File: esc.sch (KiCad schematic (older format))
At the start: 37 parts, among them IC1 C8051F330/1, P1 CONN_01X01, P2 CONN_01X01, P3 CONN_01X01

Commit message: Initial commit
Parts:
- R18, R19, R20: renamed from R?; value 470 -> 330
- gave numbers to parts that had none: 30
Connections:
- net at P5.1 (P1), Q5.3 (D), R9.1: now also Q4.2 (D)
- no-connect marks 0 -> 4

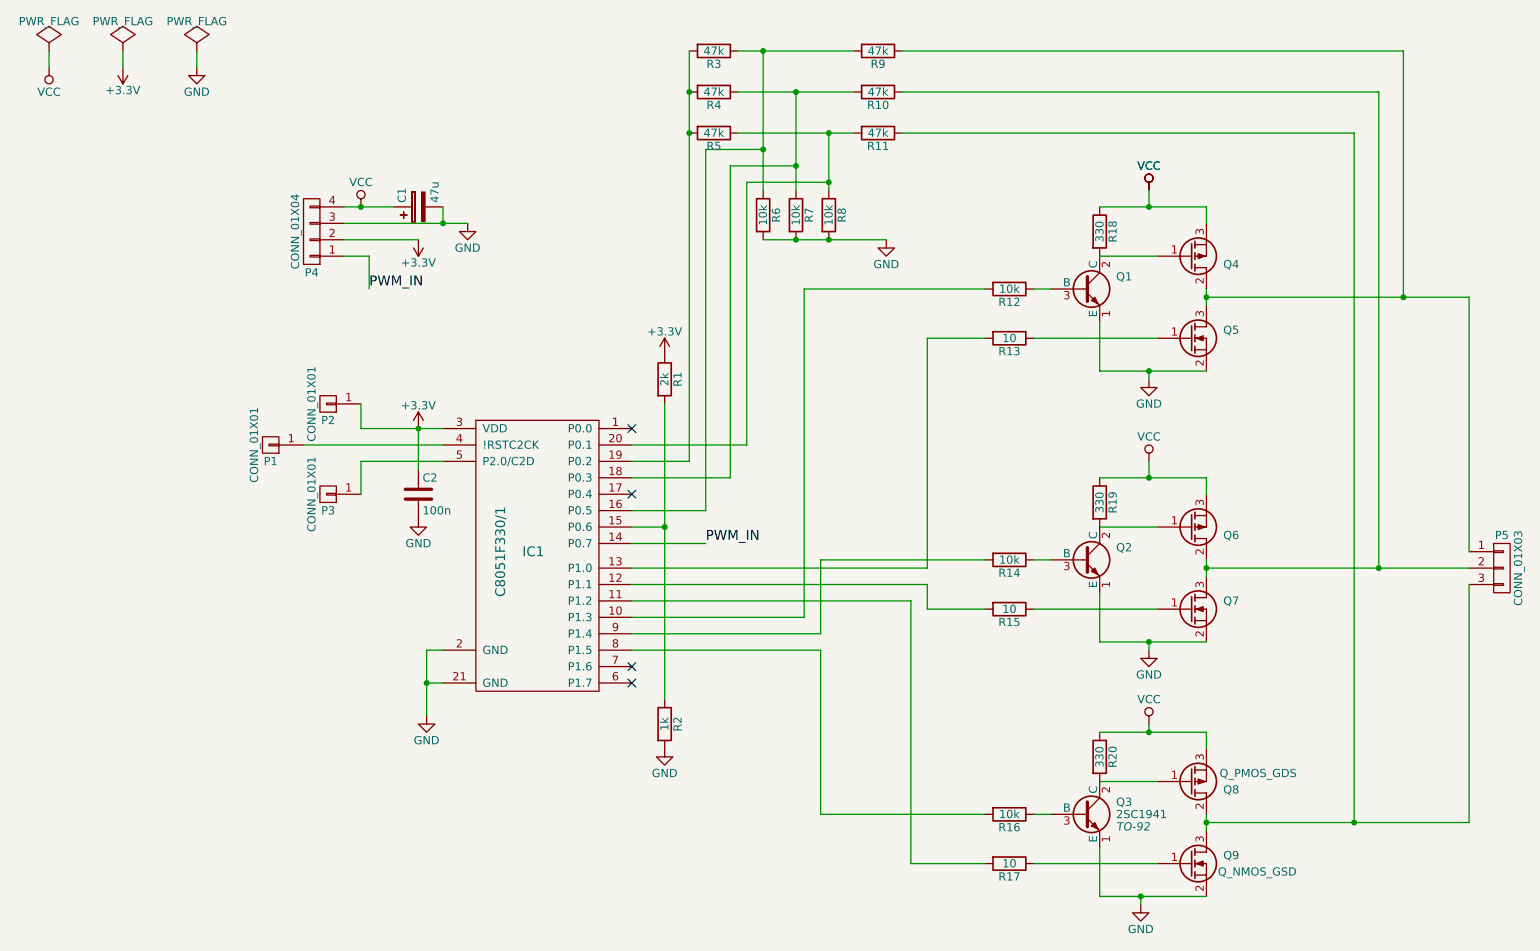
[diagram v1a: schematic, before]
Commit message: Beginning layout, breadboard test board, and BOM
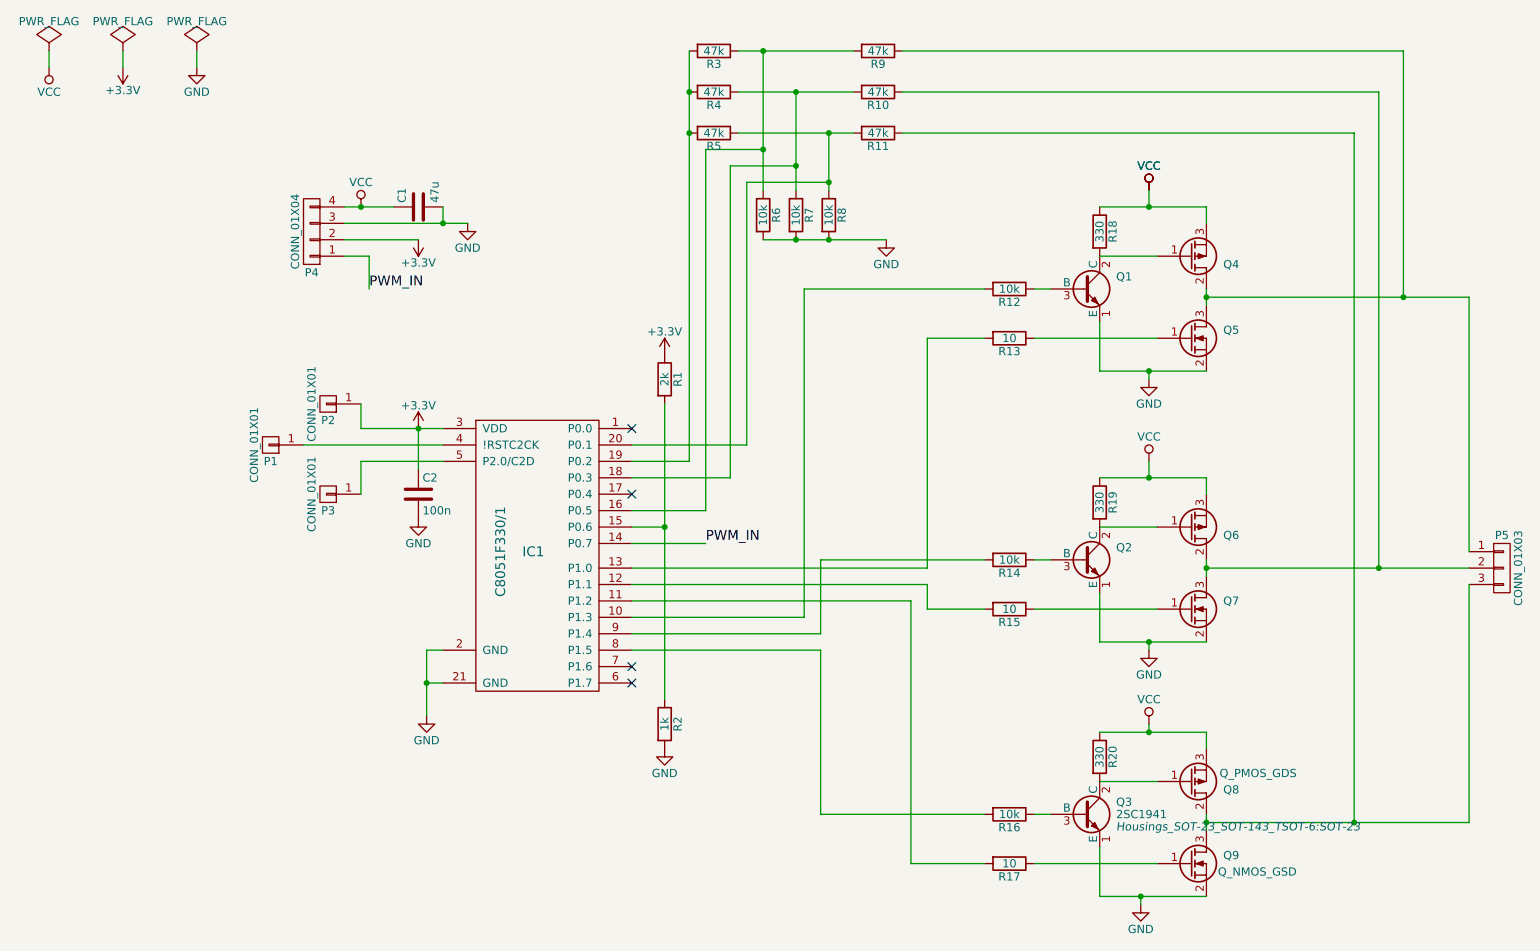
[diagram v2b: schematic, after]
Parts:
- removed C1: 47u, symbol CP
- added C1: 47u, Capacitors_SMD:C_1210, symbol C
- C2: footprint (none) -> Capacitors_SMD:C_0402
- IC1: footprint (none) -> Housings_DFN_QFN:QFN-20-1EP_4x4mm_Pitch0.5mm
- Q1, Q2, Q3: footprint TO-92 -> Housings_SOT-23_SOT-143_TSOT-6:SOT-23
- Q4, Q5, Q6, Q7, Q8, Q9: footprint (none) -> Housings_SOT-23_SOT-143_TSOT-6:SOT-23
- R1, R10, R11, R12, R13, R14, R15, R16, R17, R18, R19, R2, R20, R3, R4, R5, R6, R7, R8, R9: footprint (none) -> Resistors_SMD:R_0402
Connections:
- net GND: now also C1.2
- net VCC: now also C1.1
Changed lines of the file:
@@
 LIBS:valves
 LIBS:esc
+LIBS:esc-cache
 EELAYER 25 0
 EELAYER END
@@
 F 0 "IC1" H 3800 4150 60  0000 C CNN
 F 1 "C8051F330/1" V 3600 4150 60  0000 C CNN
-F 2 "" H 3850 4000 60  0000 C CNN
+F 2 "Housings_DFN_QFN:QFN-20-1EP_4x4mm_Pitch0.5mm" H 3850 4000 60  0001 C CNN
 F 3 "" H 3850 4000 60  0000 C CNN
 	1    3850 4000
@@
 F 0 "P2" H 2550 3050 50  0000 C CNN
 F 1 "CONN_01X01" V 2650 2950 50  0000 C CNN
-F 2 "" H 2550 2950 60  0000 C CNN
+F 2 "" H 2550 2950 60  0001 C CNN
 F 3 "" H 2550 2950 60  0000 C CNN
 	1    2550 2950
@@
 F 0 "P1" H 2200 3300 50  0000 C CNN
 F 1 "CONN_01X01" V 2300 3200 50  0000 C CNN
-F 2 "" H 2200 3200 60  0000 C CNN
+F 2 "" H 2200 3200 60  0001 C CNN
 F 3 "" H 2200 3200 60  0000 C CNN
 	1    2200 3200
@@
 F 0 "P3" H 2550 3600 50  0000 C CNN
 F 1 "CONN_01X01" V 2650 3500 50  0000 C CNN
-F 2 "" H 2550 3500 60  0000 C CNN
+F 2 "" H 2550 3500 60  0001 C CNN
 F 3 "" H 2550 3500 60  0000 C CNN
 	1    2550 3500
@@
 F 0 "P5" H 9700 4150 50  0000 C CNN
 F 1 "CONN_01X03" V 9800 3950 50  0000 C CNN
-F 2 "" H 9700 3950 60  0000 C CNN
+F 2 "" H 9700 3950 60  0001 C CNN
 F 3 "" H 9700 3950 60  0000 C CNN
 	1    9700 3950
@@
 F 0 "Q5" H 8100 2600 50  0000 R CNN
 F 1 "Q_NMOS_GSD" H 8450 2500 50  0001 R CNN
-F 2 "" H 8000 2650 29  0000 C CNN
+F 2 "Housings_SOT-23_SOT-143_TSOT-6:SOT-23" H 8000 2650 29  0001 C CNN
 F 3 "" H 7800 2550 60  0000 C CNN
 	1    7800 2550
@@
 F 0 "Q4" H 8100 2100 50  0000 R CNN
 F 1 "Q_PMOS_GDS" H 8450 2000 50  0001 R CNN
-F 2 "" H 8000 2150 29  0000 C CNN
+F 2 "Housings_SOT-23_SOT-143_TSOT-6:SOT-23" H 8000 2150 29  0001 C CNN
 F 3 "" H 7800 2050 60  0000 C CNN
 	1    7800 2050
@@
 F 0 "Q1" H 7350 2325 50  0000 L CNN
 F 1 "2SC1941" H 7350 2250 50  0001 L CNN
-F 2 "TO-92" H 7350 2175 50  0001 L CIN
+F 2 "Housings_SOT-23_SOT-143_TSOT-6:SOT-23" H 7350 2175 50  0001 L CIN
 F 3 "" H 7150 2250 50  0000 L CNN
 	1    7150 2250
@@
 F 0 "R18" V 7330 1900 50  0000 C CNN
 F 1 "330" V 7250 1900 50  0000 C CNN
-F 2 "" V 7180 1900 30  0000 C CNN
+F 2 "Resistors_SMD:R_0402" V 7180 1900 30  0001 C CNN
 F 3 "" H 7250 1900 30  0000 C CNN
 	1    7250 1900
@@
 F 0 "R12" V 6780 2250 50  0000 C CNN
 F 1 "10k" V 6700 2250 50  0000 C CNN
-F 2 "" V 6630 2250 30  0000 C CNN
+F 2 "Resistors_SMD:R_0402" V 6630 2250 30  0001 C CNN
 F 3 "" H 6700 2250 30  0000 C CNN
 	1    6700 2250
@@
 F 0 "R13" V 6780 2550 50  0000 C CNN
 F 1 "10" V 6700 2550 50  0000 C CNN
-F 2 "" V 6630 2550 30  0000 C CNN
+F 2 "Resistors_SMD:R_0402" V 6630 2550 30  0001 C CNN
 F 3 "" H 6700 2550 30  0000 C CNN
 	1    6700 2550
@@
 F 0 "Q6" H 8100 3750 50  0000 R CNN
 F 1 "Q_PMOS_GDS" H 8450 3650 50  0001 R CNN
-F 2 "" H 8000 3800 29  0000 C CNN
+F 2 "Housings_SOT-23_SOT-143_TSOT-6:SOT-23" H 8000 3800 29  0001 C CNN
 F 3 "" H 7800 3700 60  0000 C CNN
 	1    7800 3700
@@
 F 0 "Q7" H 8100 4250 50  0000 R CNN
 F 1 "Q_NMOS_GSD" H 8450 4150 50  0001 R CNN
-F 2 "" H 8000 4300 29  0000 C CNN
+F 2 "Housings_SOT-23_SOT-143_TSOT-6:SOT-23" H 8000 4300 29  0001 C CNN
 F 3 "" H 7800 4200 60  0000 C CNN
 	1    7800 4200
@@
 F 0 "Q2" H 7350 3975 50  0000 L CNN
 F 1 "2SC1941" H 7350 3900 50  0001 L CNN
-F 2 "TO-92" H 7350 3825 50  0001 L CIN
+F 2 "Housings_SOT-23_SOT-143_TSOT-6:SOT-23" H 7350 3825 50  0001 L CIN
 F 3 "" H 7150 3900 50  0000 L CNN
 	1    7150 3900
@@
 F 0 "R19" V 7330 3550 50  0000 C CNN
 F 1 "330" V 7250 3550 50  0000 C CNN
-F 2 "" V 7180 3550 30  0000 C CNN
+F 2 "Resistors_SMD:R_0402" V 7180 3550 30  0001 C CNN
 F 3 "" H 7250 3550 30  0000 C CNN
 	1    7250 3550
@@
 F 0 "R14" V 6780 3900 50  0000 C CNN
 F 1 "10k" V 6700 3900 50  0000 C CNN
-F 2 "" V 6630 3900 30  0000 C CNN
+F 2 "Resistors_SMD:R_0402" V 6630 3900 30  0001 C CNN
 F 3 "" H 6700 3900 30  0000 C CNN
 	1    6700 3900
@@
 F 0 "R15" V 6780 4200 50  0000 C CNN
 F 1 "10" V 6700 4200 50  0000 C CNN
-F 2 "" V 6630 4200 30  0000 C CNN
+F 2 "Resistors_SMD:R_0402" V 6630 4200 30  0001 C CNN
 F 3 "" H 6700 4200 30  0000 C CNN
 	1    6700 4200
@@
 F 0 "Q8" H 8100 5300 50  0000 R CNN
 F 1 "Q_PMOS_GDS" H 8450 5200 50  0000 R CNN
-F 2 "" H 8000 5350 29  0000 C CNN
+F 2 "Housings_SOT-23_SOT-143_TSOT-6:SOT-23" H 8000 5350 29  0001 C CNN
 F 3 "" H 7800 5250 60  0000 C CNN
 	1    7800 5250
@@
 F 0 "Q9" H 8100 5800 50  0000 R CNN
 F 1 "Q_NMOS_GSD" H 8450 5700 50  0000 R CNN
-F 2 "" H 8000 5850 29  0000 C CNN
+F 2 "Housings_SOT-23_SOT-143_TSOT-6:SOT-23" H 8000 5850 29  0001 C CNN
 F 3 "" H 7800 5750 60  0000 C CNN
 	1    7800 5750
@@
 F 0 "R20" V 7330 5100 50  0000 C CNN
 F 1 "330" V 7250 5100 50  0000 C CNN
-F 2 "" V 7180 5100 30  0000 C CNN
+F 2 "Resistors_SMD:R_0402" V 7180 5100 30  0001 C CNN
 F 3 "" H 7250 5100 30  0000 C CNN
 	1    7250 5100
@@
 F 0 "Q3" H 7350 5525 50  0000 L CNN
 F 1 "2SC1941" H 7350 5450 50  0000 L CNN
-F 2 "TO-92" H 7350 5375 50  0000 L CIN
+F 2 "Housings_SOT-23_SOT-143_TSOT-6:SOT-23" H 7350 5375 50  0000 L CIN
 F 3 "" H 7150 5450 50  0000 L CNN
 	1    7150 5450
@@
 F 0 "R16" V 6780 5450 50  0000 C CNN
 F 1 "10k" V 6700 5450 50  0000 C CNN
-F 2 "" V 6630 5450 30  0000 C CNN
+F 2 "Resistors_SMD:R_0402" V 6630 5450 30  0001 C CNN
 F 3 "" H 6700 5450 30  0000 C CNN
 	1    6700 5450
@@
 F 0 "R17" V 6780 5750 50  0000 C CNN
 F 1 "10" V 6700 5750 50  0000 C CNN
-F 2 "" V 6630 5750 30  0000 C CNN
+F 2 "Resistors_SMD:R_0402" V 6630 5750 30  0001 C CNN
 F 3 "" H 6700 5750 30  0000 C CNN
 	1    6700 5750
@@
 F 0 "R11" V 5980 1300 50  0000 C CNN
 F 1 "47k" V 5900 1300 50  0000 C CNN
-F 2 "" V 5830 1300 30  0000 C CNN
+F 2 "Resistors_SMD:R_0402" V 5830 1300 30  0001 C CNN
 F 3 "" H 5900 1300 30  0000 C CNN
 	1    5900 1300
@@
 F 0 "R10" V 5980 1050 50  0000 C CNN
 F 1 "47k" V 5900 1050 50  0000 C CNN
-F 2 "" V 5830 1050 30  0000 C CNN
+F 2 "Resistors_SMD:R_0402" V 5830 1050 30  0001 C CNN
 F 3 "" H 5900 1050 30  0000 C CNN
 	1    5900 1050
@@
 F 0 "R9" V 5980 800 50  0000 C CNN
 F 1 "47k" V 5900 800 50  0000 C CNN
-F 2 "" V 5830 800 30  0000 C CNN
+F 2 "Resistors_SMD:R_0402" V 5830 800 30  0001 C CNN
 F 3 "" H 5900 800 30  0000 C CNN
 	1    5900 800
@@
 F 0 "R8" V 5680 1800 50  0000 C CNN
 F 1 "10k" V 5600 1800 50  0000 C CNN
-F 2 "" V 5530 1800 30  0000 C CNN
+F 2 "Resistors_SMD:R_0402" V 5530 1800 30  0001 C CNN
 F 3 "" H 5600 1800 30  0000 C CNN
 	1    5600 1800
@@
 F 0 "R7" V 5480 1800 50  0000 C CNN
 F 1 "10k" V 5400 1800 50  0000 C CNN
-F 2 "" V 5330 1800 30  0000 C CNN
+F 2 "Resistors_SMD:R_0402" V 5330 1800 30  0001 C CNN
 F 3 "" H 5400 1800 30  0000 C CNN
 	1    5400 1800
@@
 F 0 "R6" V 5280 1800 50  0000 C CNN
 F 1 "10k" V 5200 1800 50  0000 C CNN
-F 2 "" V 5130 1800 30  0000 C CNN
+F 2 "Resistors_SMD:R_0402" V 5130 1800 30  0001 C CNN
 F 3 "" H 5200 1800 30  0000 C CNN
 	1    5200 1800
@@
 F 0 "R3" V 4980 800 50  0000 C CNN
 F 1 "47k" V 4900 800 50  0000 C CNN
-F 2 "" V 4830 800 30  0000 C CNN
+F 2 "Resistors_SMD:R_0402" V 4830 800 30  0001 C CNN
 F 3 "" H 4900 800 30  0000 C CNN
 	1    4900 800
@@
 F 0 "R4" V 4980 1050 50  0000 C CNN
 F 1 "47k" V 4900 1050 50  0000 C CNN
-F 2 "" V 4830 1050 30  0000 C CNN
+F 2 "Resistors_SMD:R_0402" V 4830 1050 30  0001 C CNN
 F 3 "" H 4900 1050 30  0000 C CNN
 	1    4900 1050
@@
 F 0 "R5" V 4980 1300 50  0000 C CNN
 F 1 "47k" V 4900 1300 50  0000 C CNN
-F 2 "" V 4830 1300 30  0000 C CNN
+F 2 "Resistors_SMD:R_0402" V 4830 1300 30  0001 C CNN
 F 3 "" H 4900 1300 30  0000 C CNN
 	1    4900 1300
@@
 F 0 "R1" V 4680 2800 50  0000 C CNN
 F 1 "2k" V 4600 2800 50  0000 C CNN
-F 2 "" V 4530 2800 30  0000 C CNN
+F 2 "Resistors_SMD:R_0402" V 4530 2800 30  0001 C CNN
 F 3 "" H 4600 2800 30  0000 C CNN
 	1    4600 2800
@@
 F 0 "R2" V 4680 4900 50  0000 C CNN
 F 1 "1k" V 4600 4900 50  0000 C CNN
-F 2 "" V 4530 4900 30  0000 C CNN
+F 2 "Resistors_SMD:R_0402" V 4530 4900 30  0001 C CNN
 F 3 "" H 4600 4900 30  0000 C CNN
 	1    4600 4900
@@
 F 0 "P4" H 2450 2150 50  0000 C CNN
 F 1 "CONN_01X04" V 2550 1900 50  0000 C CNN
-F 2 "" H 2450 1900 60  0000 C CNN
+F 2 "" H 2450 1900 60  0001 C CNN
 F 3 "" H 2450 1900 60  0000 C CNN
 	1    2450 1900
@@
 F 0 "C2" H 3125 3600 50  0000 L CNN
 F 1 "100n" H 3125 3400 50  0000 L CNN
-F 2 "" H 3138 3350 30  0000 C CNN
+F 2 "Capacitors_SMD:C_0402" H 3138 3350 30  0001 C CNN
 F 3 "" H 3100 3500 60  0000 C CNN
 	1    3100 3500
@@
 	3250 4650 3150 4650
 Connection ~ 3150 4650
-$Comp
-L CP C1
-U 1 1 558941D4
-P 3100 1750
-F 0 "C1" H 3125 1850 50  0000 L CNN
-F 1 "47u" H 3125 1650 50  0000 L CNN
-F 2 "" H 3138 1600 30  0000 C CNN
-F 3 "" H 3100 1750 60  0000 C CNN
-	1    3100 1750
-	0    -1   -1   0
-$EndComp
 Wire Wire Line
 	2650 1950 3100 1950
@@
 NoConn ~ 4400 4550
 NoConn ~ 4400 4650
+$Comp
+L C C1
+U 1 1 558A1CD7
+P 3100 1750
+F 0 "C1" H 3125 1850 50  0000 L CNN
+F 1 "47u" H 3125 1650 50  0000 L CNN
+F 2 "Capacitors_SMD:C_1210" H 3138 1600 30  0001 C CNN
+F 3 "" H 3100 1750 60  0000 C CNN
+	1    3100 1750
+	0    -1   -1   0
+$EndComp
 $EndSCHEMATC

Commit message: Missed some file saves in last commit
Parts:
- P1, P2, P3: footprint (none) -> esc:test_pin
- P4: footprint (none) -> Pin_Headers:Pin_Header_Straight_1x04
- P5: footprint (none) -> Pin_Headers:Pin_Header_Straight_1x03
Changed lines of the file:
@@
 F 0 "P2" H 2550 3050 50  0000 C CNN
 F 1 "CONN_01X01" V 2650 2950 50  0000 C CNN
-F 2 "" H 2550 2950 60  0001 C CNN
+F 2 "esc:test_pin" H 2550 2950 60  0001 C CNN
 F 3 "" H 2550 2950 60  0000 C CNN
 	1    2550 2950
@@
 F 0 "P1" H 2200 3300 50  0000 C CNN
 F 1 "CONN_01X01" V 2300 3200 50  0000 C CNN
-F 2 "" H 2200 3200 60  0001 C CNN
+F 2 "esc:test_pin" H 2200 3200 60  0001 C CNN
 F 3 "" H 2200 3200 60  0000 C CNN
 	1    2200 3200
@@
 F 0 "P3" H 2550 3600 50  0000 C CNN
 F 1 "CONN_01X01" V 2650 3500 50  0000 C CNN
-F 2 "" H 2550 3500 60  0001 C CNN
+F 2 "esc:test_pin" H 2550 3500 60  0001 C CNN
 F 3 "" H 2550 3500 60  0000 C CNN
 	1    2550 3500
@@
 F 0 "P5" H 9700 4150 50  0000 C CNN
 F 1 "CONN_01X03" V 9800 3950 50  0000 C CNN
-F 2 "" H 9700 3950 60  0001 C CNN
+F 2 "Pin_Headers:Pin_Header_Straight_1x03" H 9700 3950 60  0001 C CNN
 F 3 "" H 9700 3950 60  0000 C CNN
 	1    9700 3950
@@
 F 0 "P4" H 2450 2150 50  0000 C CNN
 F 1 "CONN_01X04" V 2550 1900 50  0000 C CNN
-F 2 "" H 2450 1900 60  0001 C CNN
+F 2 "Pin_Headers:Pin_Header_Straight_1x04" H 2450 1900 60  0001 C CNN
 F 3 "" H 2450 1900 60  0000 C CNN
 	1    2450 1900
